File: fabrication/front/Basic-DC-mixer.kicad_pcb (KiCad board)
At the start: 2 copper layers, 40 x 128 mm, 4 parts

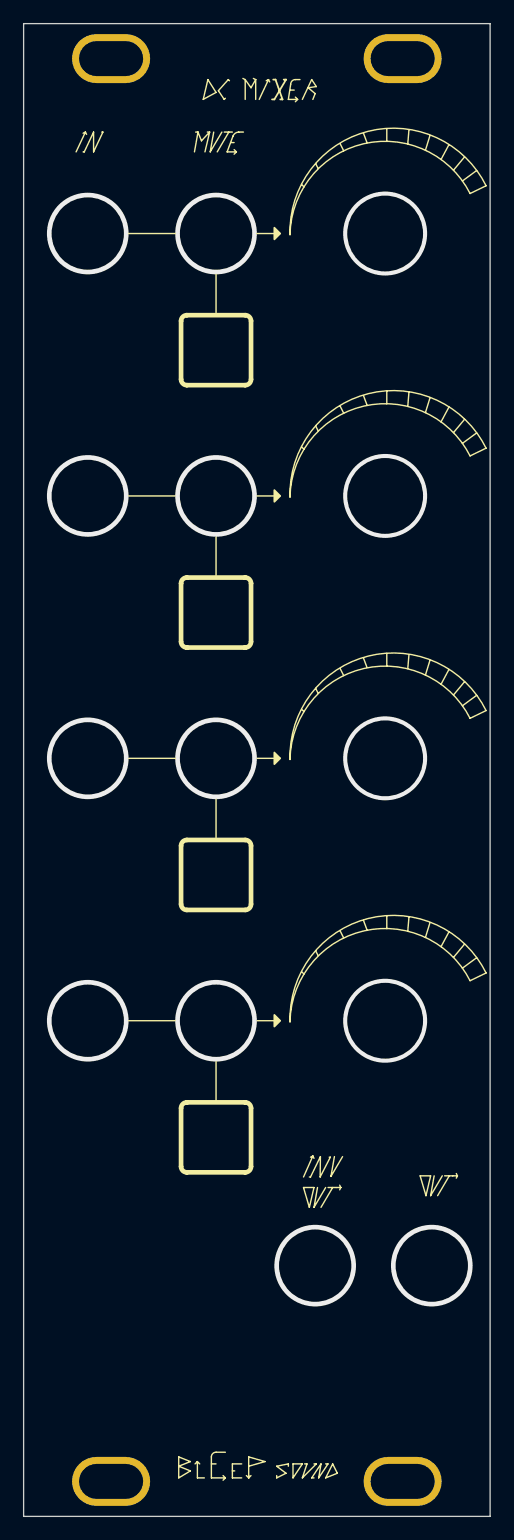
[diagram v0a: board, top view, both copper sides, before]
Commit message: update silkscreen and hole diameter
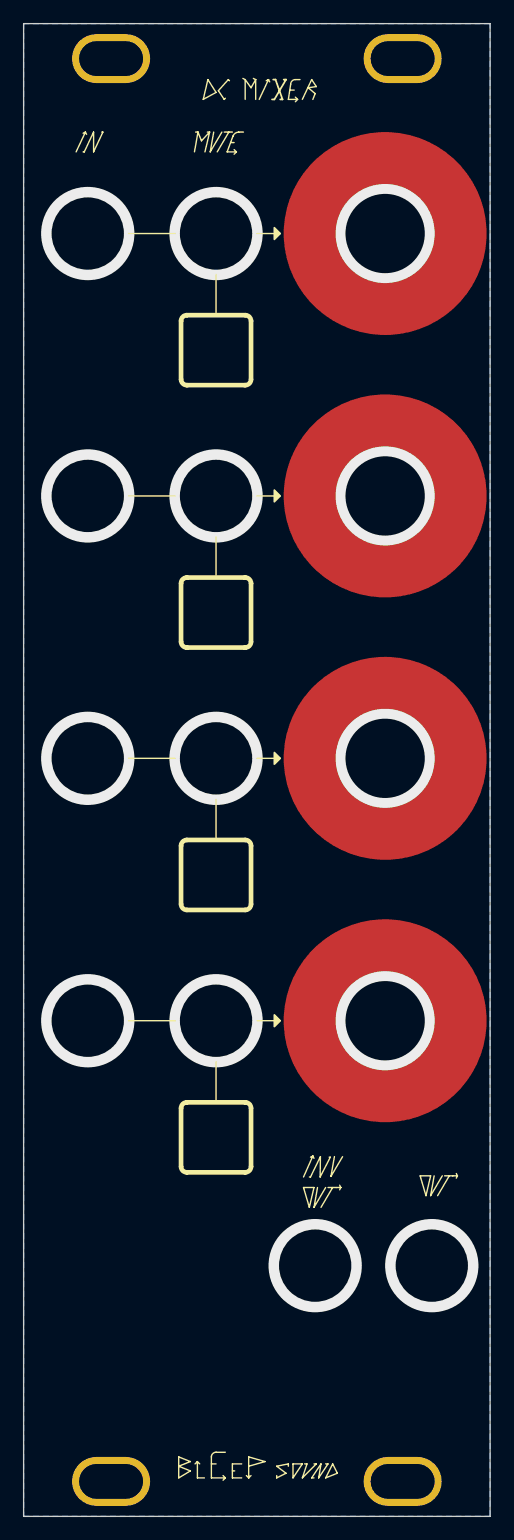
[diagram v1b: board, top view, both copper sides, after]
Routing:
- net GND: vias 0 -> 10
- net (no net): vias 14 -> 4
- added copper zone on B.Cu, net GND
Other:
- board text added: "DC coupled mixer"
- board text added: "V1.1 BleepSound 2023"

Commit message: update mixer to v1.2, update repo organization
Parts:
- added G***: LOGO, LOGO, F.Cu at (102.3, 138.7)
- added G***: LOGO, LOGO, F.Cu at (83.5, 139.0)
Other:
- board text added: "V1.2 BleepSound 2023"
- board text removed: "V1.1 BleepSound 2023"
